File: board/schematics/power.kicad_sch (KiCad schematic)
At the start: 9 parts, among them J3 Power Input, U2 LM317_TO-220

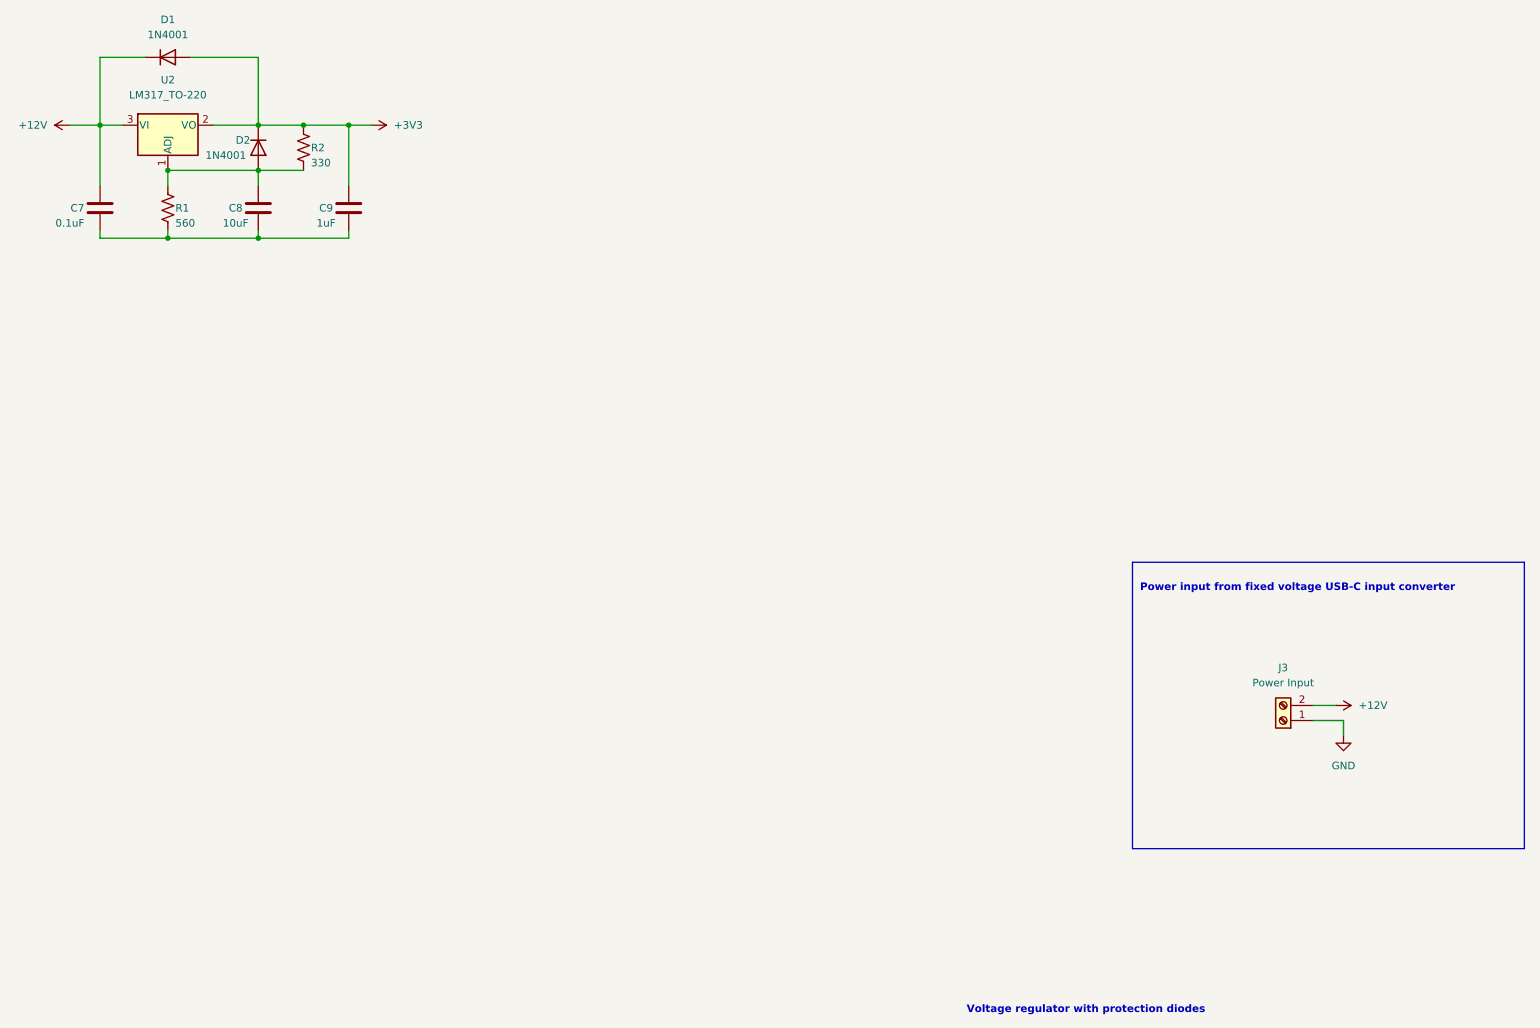
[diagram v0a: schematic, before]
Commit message: feat: update sheet layout
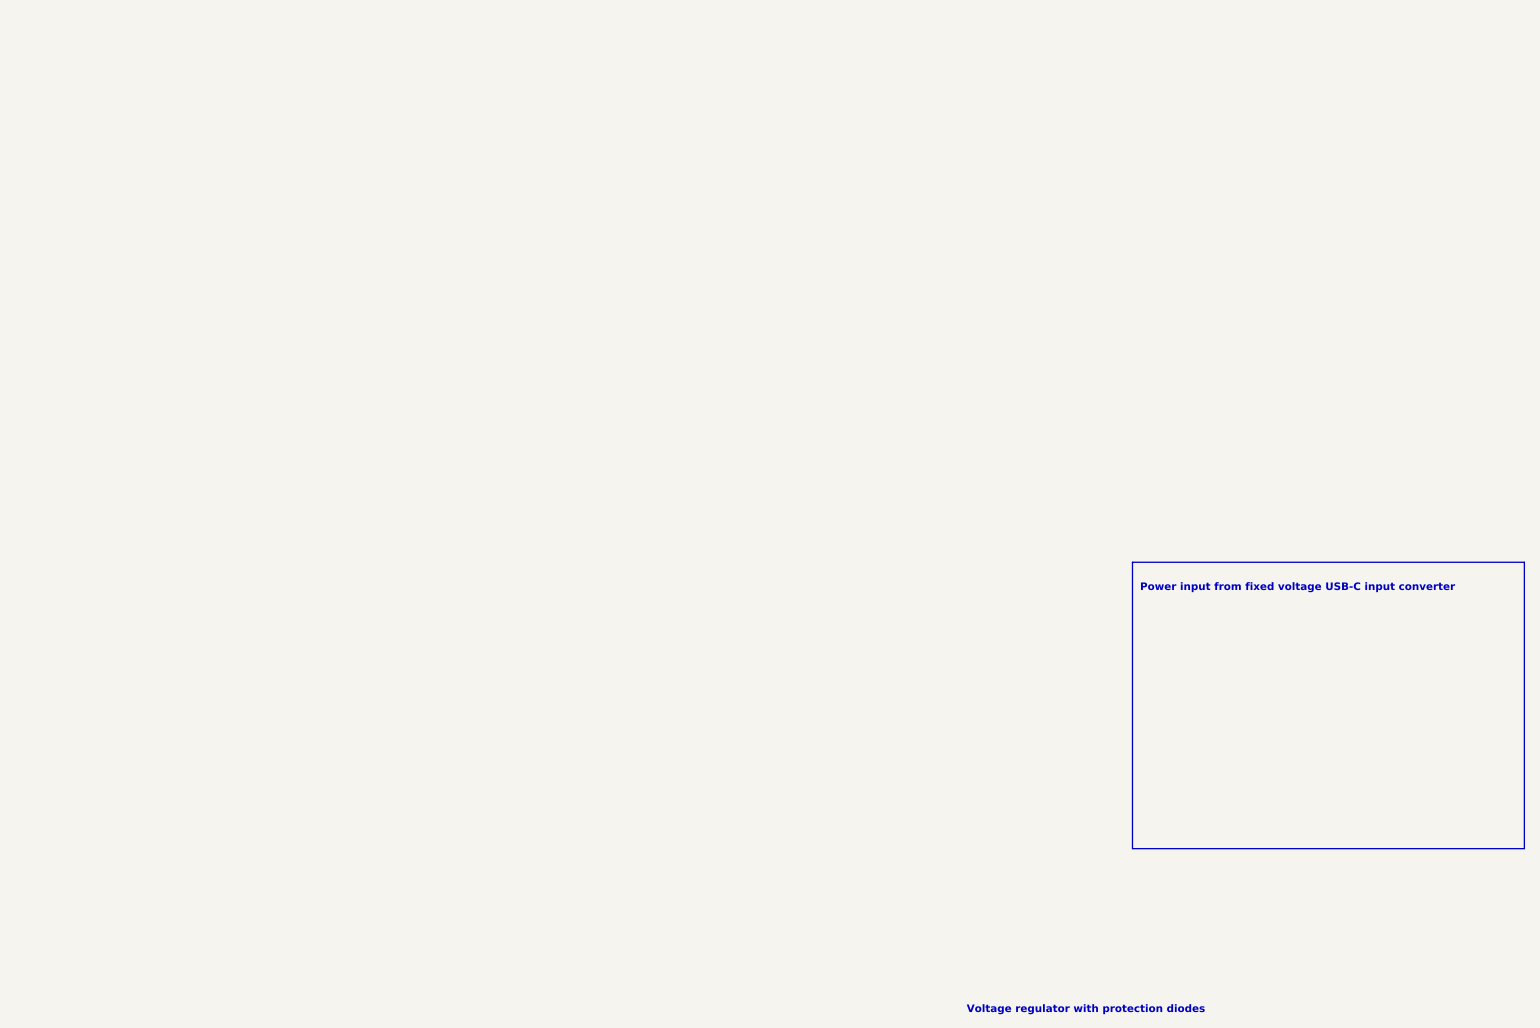
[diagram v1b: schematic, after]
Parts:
- removed C7: 0.1uF, symbol Device:C
- removed C8: 10uF, symbol Device:C
- removed C9: 1uF, symbol Device:C
- removed D1, D2: 1N4001, Diode_THT:D_DO-41_SOD81_P10.16mm_Horizontal, symbol Diode:1N4001
- removed J3: Power Input, symbol Connector:Screw_Terminal_01x02
- removed R1: 560, symbol Device:R_US
- removed R2: 330, symbol Device:R_US
- removed U2: LM317_TO-220, Package_TO_SOT_THT:TO-220-3_Vertical, symbol Regulator_Linear:LM317_TO-220
